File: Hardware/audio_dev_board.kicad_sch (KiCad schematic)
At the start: 0 parts

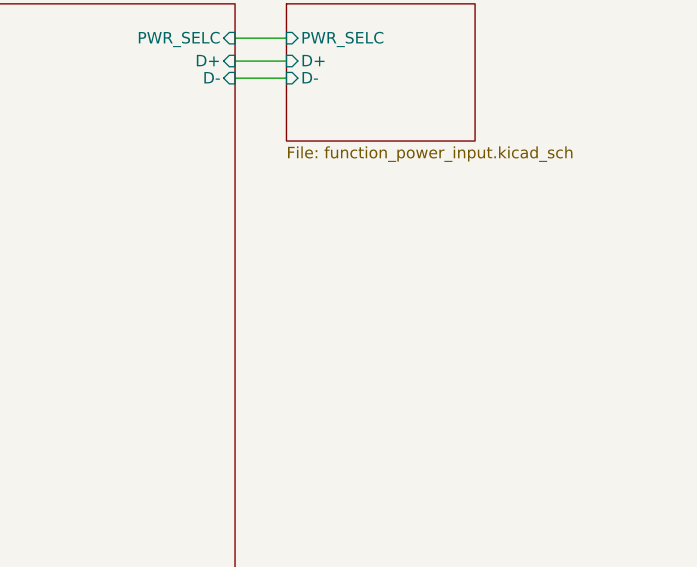
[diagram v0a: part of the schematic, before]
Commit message: Added CODEC symbol, started routing
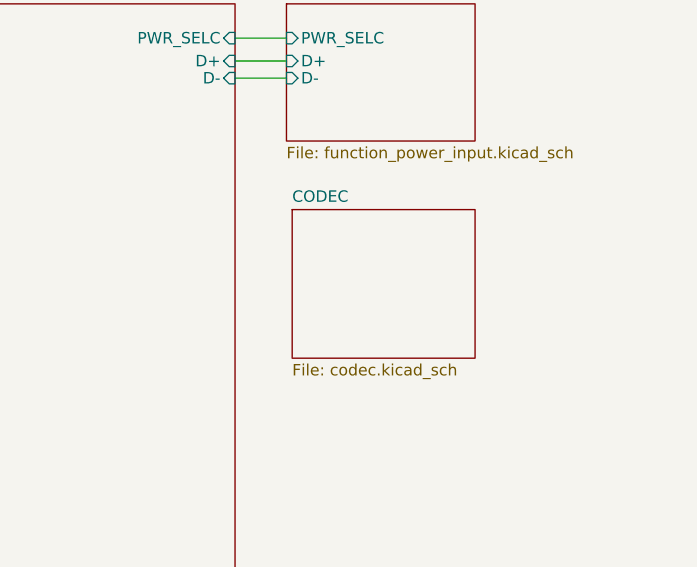
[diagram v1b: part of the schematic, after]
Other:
- added sheet CODEC (codec.kicad_sch)
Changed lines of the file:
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@@
+	)
+	(sheet
+		(at 101.6 43.18)
+		(size 20.32 16.51)
+		(fields_autoplaced yes)
+		(stroke
+			(width 0.1524)
+			(type solid)
+		)
+		(fill
+			(color 0 0 0 0.0000)
+		)
+		(property "Sheetname" "CODEC"
+			(at 101.6 42.4684 0)
+			(effects
+				(font
+					(size 1.27 1.27)
+				)
+				(justify left bottom)
+			)
+		)
+		(property "Sheetfile" "codec.kicad_sch"
+			(at 101.6 60.2746 0)
+			(effects
+				(font
+					(size 1.27 1.27)
+				)
+				(justify left top)
+			)
+		)
+		(instances
+			(project "audio_dev_board"
+				(path "/12d3b0ce-758b-4939-919d-4f42b7bd226b"
+					(page "4")
+				)
+			)
+		)
 	)
 	(sheet

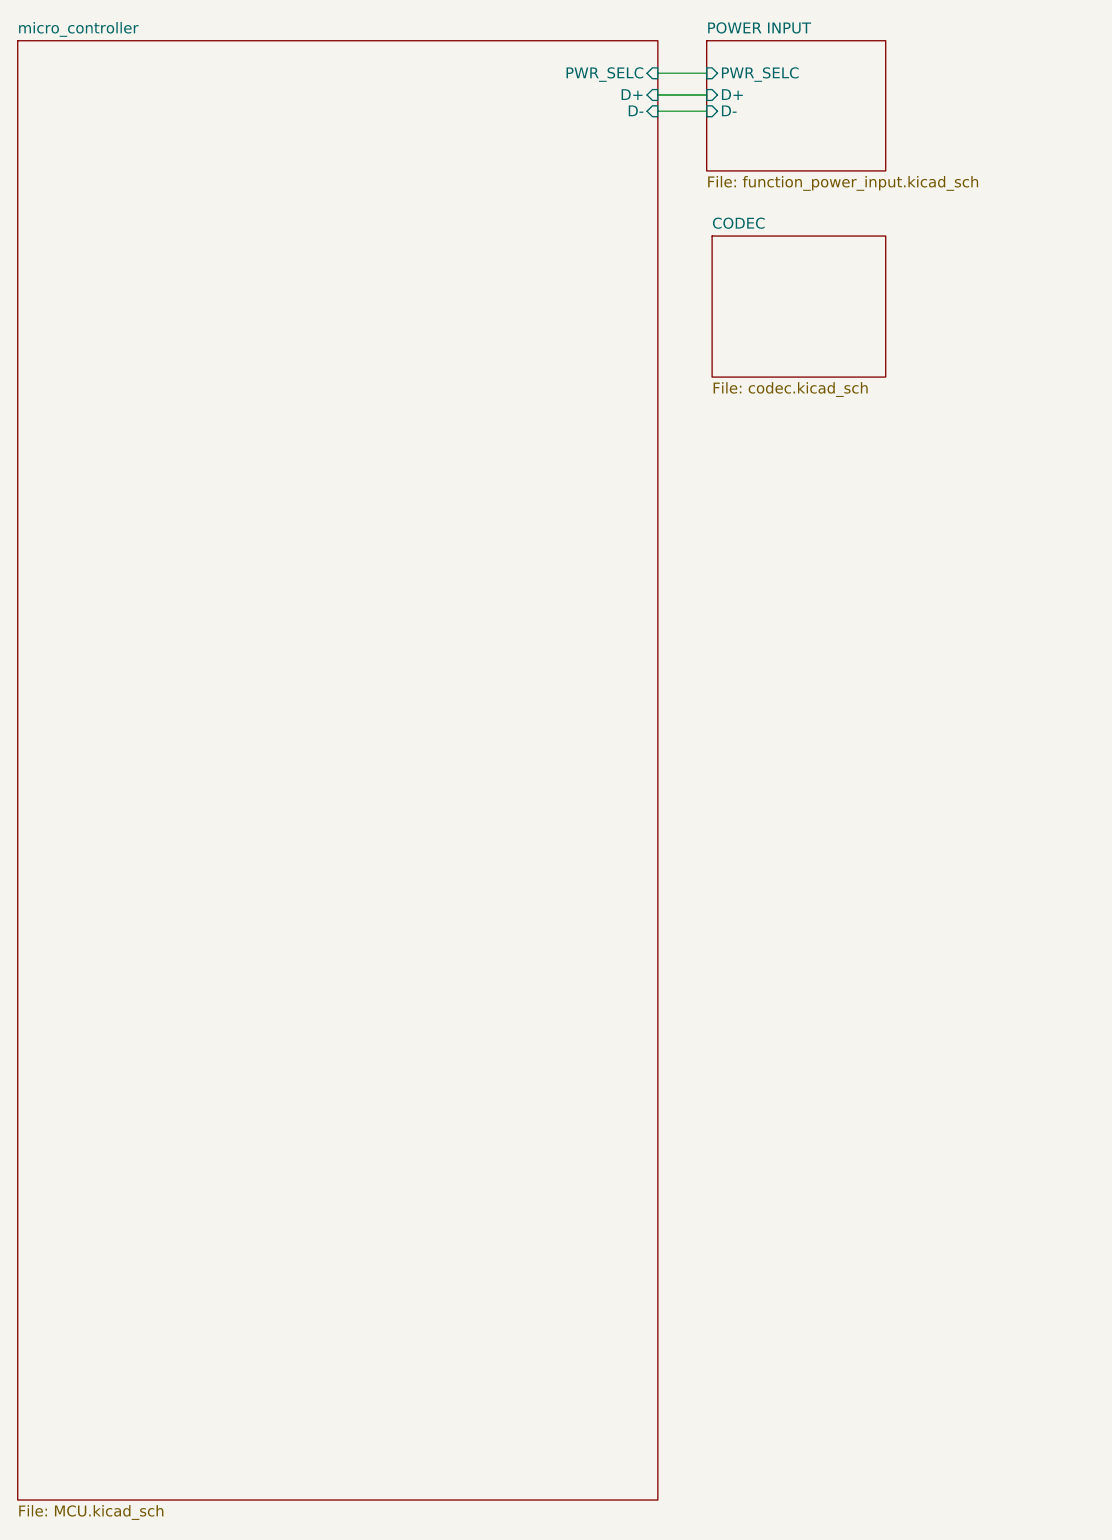
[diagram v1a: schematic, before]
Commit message: connected micro to codec and debug leds
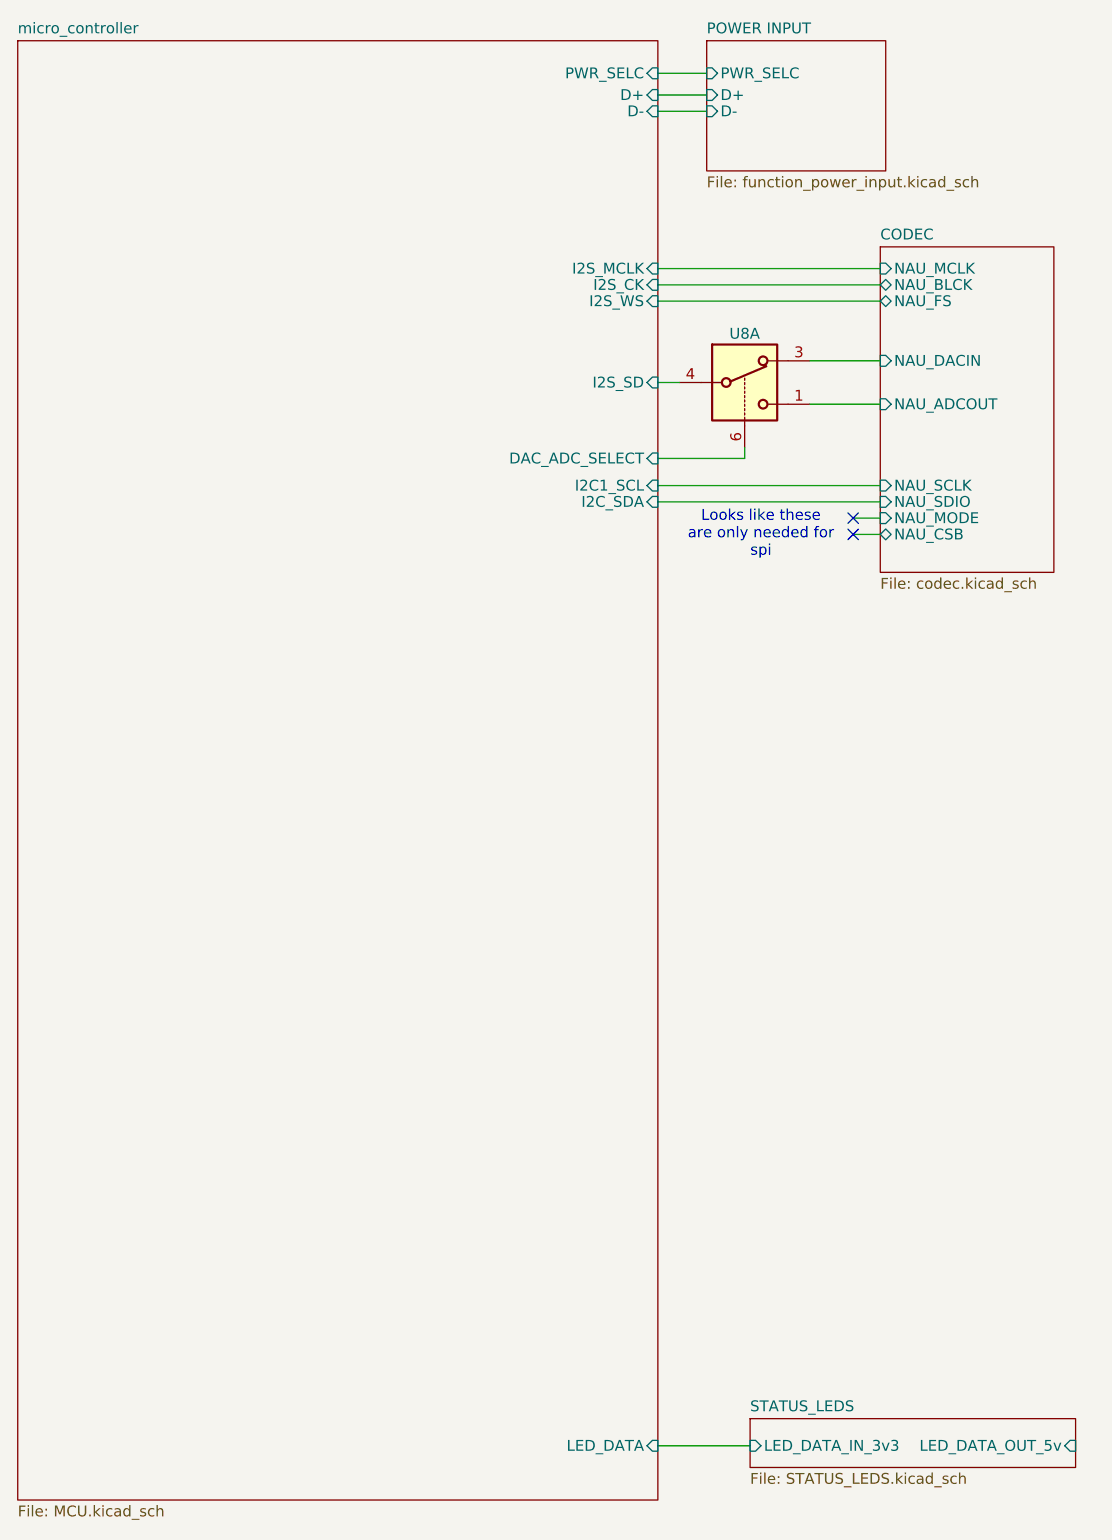
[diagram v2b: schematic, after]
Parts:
- added U8: FSA3157P6X, Package_TO_SOT_SMD:SOT-363_SC-70-6, symbol Analog_Switch:FSA3157P6X
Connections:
- new net CODEC/NAU_ADCOUT: U8.1
- new net CODEC/NAU_DACIN: U8.3
- new net micro_controller/DAC_ADC_SELECT: U8.6
- new net micro_controller/I2S_SD: U8.4
- no-connect marks 0 -> 2
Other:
- added sheet STATUS_LEDS (STATUS_LEDS.kicad_sch)
- sheet CODEC ports: added NAU_ADCOUT, NAU_BLCK, NAU_CSB, NAU_DACIN, NAU_FS, NAU_MCLK, NAU_MODE, NAU_SCLK, NAU_SDIO; removed none
- sheet micro_controller ports: added DAC_ADC_SELECT, I2C1_SCL, I2C_SDA, I2S_CK, I2S_MCLK, I2S_SD, I2S_WS, LED_DATA; removed none
- note added: "Looks like these are only needed for spi"
